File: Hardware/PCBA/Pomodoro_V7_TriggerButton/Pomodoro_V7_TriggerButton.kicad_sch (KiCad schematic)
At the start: 2 parts, among them J1 Conn_01x02_Pin, SW1 SW_Push

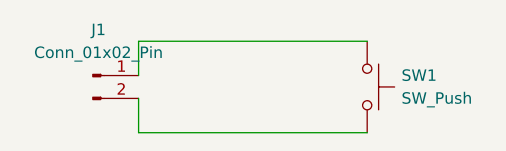
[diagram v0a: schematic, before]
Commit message: added the selector wheel, changed the Connectors on the Trigger Button to move the assemlby closer together
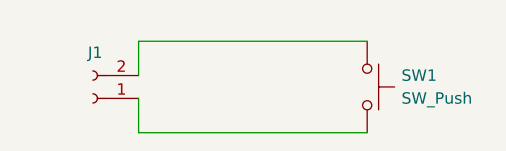
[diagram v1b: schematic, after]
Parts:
- removed J1: Conn_01x02_Pin, Connector_PinHeader_2.54mm:PinHeader_1x02_P2.54mm_Horizontal, symbol Connector:Conn_01x02_Pin
- added J1: Conn_01x02_Socket, Connector_PinSocket_2.54mm:PinSocket_1x02_P2.54mm_Vertical, symbol Connector:Conn_01x02_Socket
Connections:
- net at SW1.1: now also J1.2 (Pin_2)
- net at SW1.2: now also J1.1 (Pin_1)
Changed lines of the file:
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@@
+	)
+	(symbol
+		(lib_id "Connector:Conn_01x02_Socket")
+		(at 95.25 68.58 180)
+		(unit 1)
+		(exclude_from_sim no)
+		(in_bom yes)
+		(on_board yes)
+		(dnp no)
+		(property "Reference" "J1"
+			(at 95.504 63.5 0)
+			(effects
+				(font
+					(size 1.27 1.27)
+				)
+			)
+		)
+		(property "Value" "Conn_01x02_Socket"
+			(at 95.885 63.5 0)
+			(effects
+				(font
+					(size 1.27 1.27)
+				)
+				(hide yes)
+			)
+		)
+		(property "Footprint" "Connector_PinSocket_2.54mm:PinSocket_1x02_P2.54mm_Vertical"
+			(at 95.25 68.58 0)
+			(effects
+				(font
+					(size 1.27 1.27)
+				)
+				(hide yes)
+			)
+		)
+		(property "Datasheet" "~"
+			(at 95.25 68.58 0)
+			(effects
+				(font
+					(size 1.27 1.27)
+				)
+				(hide yes)
+			)
+		)
+		(property "Description" "Generic connector, single row, 01x02, script generated"
+			(at 95.25 68.58 0)
+			(effects
+				(font
+					(size 1.27 1.27)
+				)
+				(hide yes)
+			)
+		)
+		(pin "2"
+		)
+		(pin "1"
+		)
+		(instances
+			(project "Pomodoro_V7_TriggerButton"
+				(path "/1d0650ba-ca90-4715-a176-98a9d64b4b3f"
+					(reference "J1")
+					(unit 1)
+				)
+			)
+		)
 	)
 	(symbol
@@
 					(unit 1)
 				)
-			)
-		)
-	)
-	(symbol
-		(lib_id "Connector:Conn_01x02_Pin")
-		(at 95.25 66.04 0)
-		(unit 1)
-		(exclude_from_sim no)
-		(in_bom yes)
-		(on_board yes)
-		(dnp no)
-		(fields_autoplaced yes)
-		(property "Reference" "J1"
-			(at 95.885 60.96 0)
-			(effects
-				(font
-					(size 1.27 1.27)
-				)
-			)
-		)
-		(property "Value" "Conn_01x02_Pin"
-			(at 95.885 63.5 0)
-			(effects
-				(font
-					(size 1.27 1.27)
-				)
-			)
-		)
-		(property "Footprint" "Connector_PinHeader_2.54mm:PinHeader_1x02_P2.54mm_Horizontal"
-			(at 95.25 66.04 0)
-			(effects
-				(font
-					(size 1.27 1.27)
-				)
-				(hide yes)
-			)
-		)
-		(property "Datasheet" "~"
-			(at 95.25 66.04 0)
-			(effects
-				(font
-					(size 1.27 1.27)
-				)
-				(hide yes)
-			)
-		)
-		(property "Description" "Generic connector, single row, 01x02, script generated"
-			(at 95.25 66.04 0)
-			(effects
-				(font
-					(size 1.27 1.27)
-				)
-				(hide yes)
-			)
-		)
-		(pin "1"
-		)
-		(pin "2"
-		)
-		(instances
-			(project "Pomodoro_V7_TriggerButton"
-				(path "/1d0650ba-ca90-4715-a176-98a9d64b4b3f"
-					(reference "J1")
-					(unit 1)
-				)
